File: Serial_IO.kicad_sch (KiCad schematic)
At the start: 39 parts

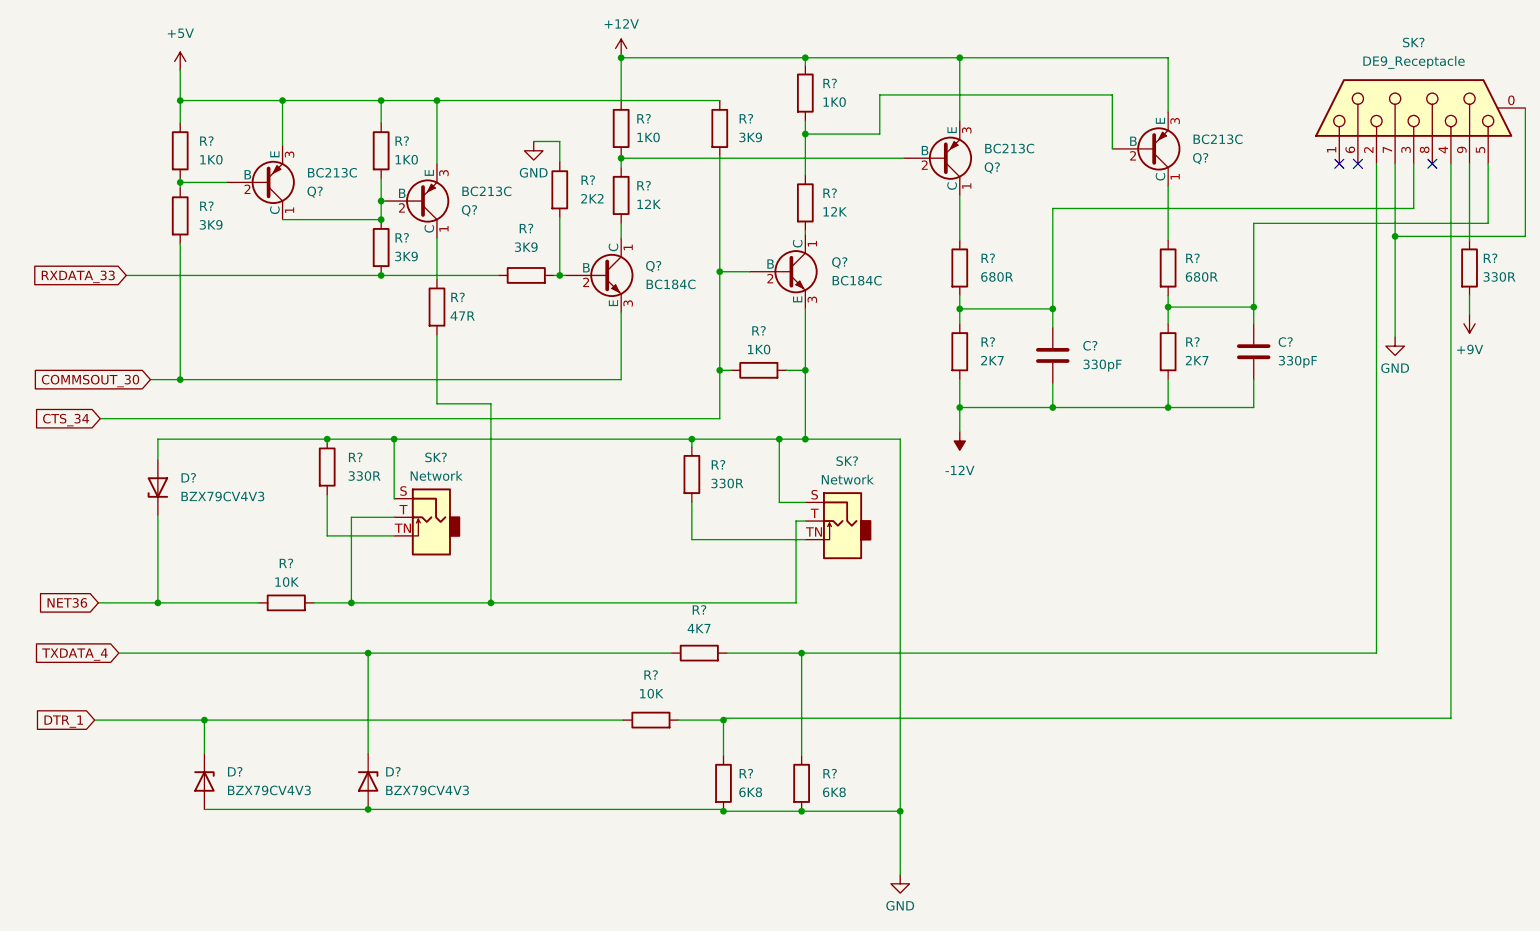
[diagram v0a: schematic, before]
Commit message: Add files via upload
Updated with Kicad 9. Now includes bom/ibom.html (Interactice BOM)
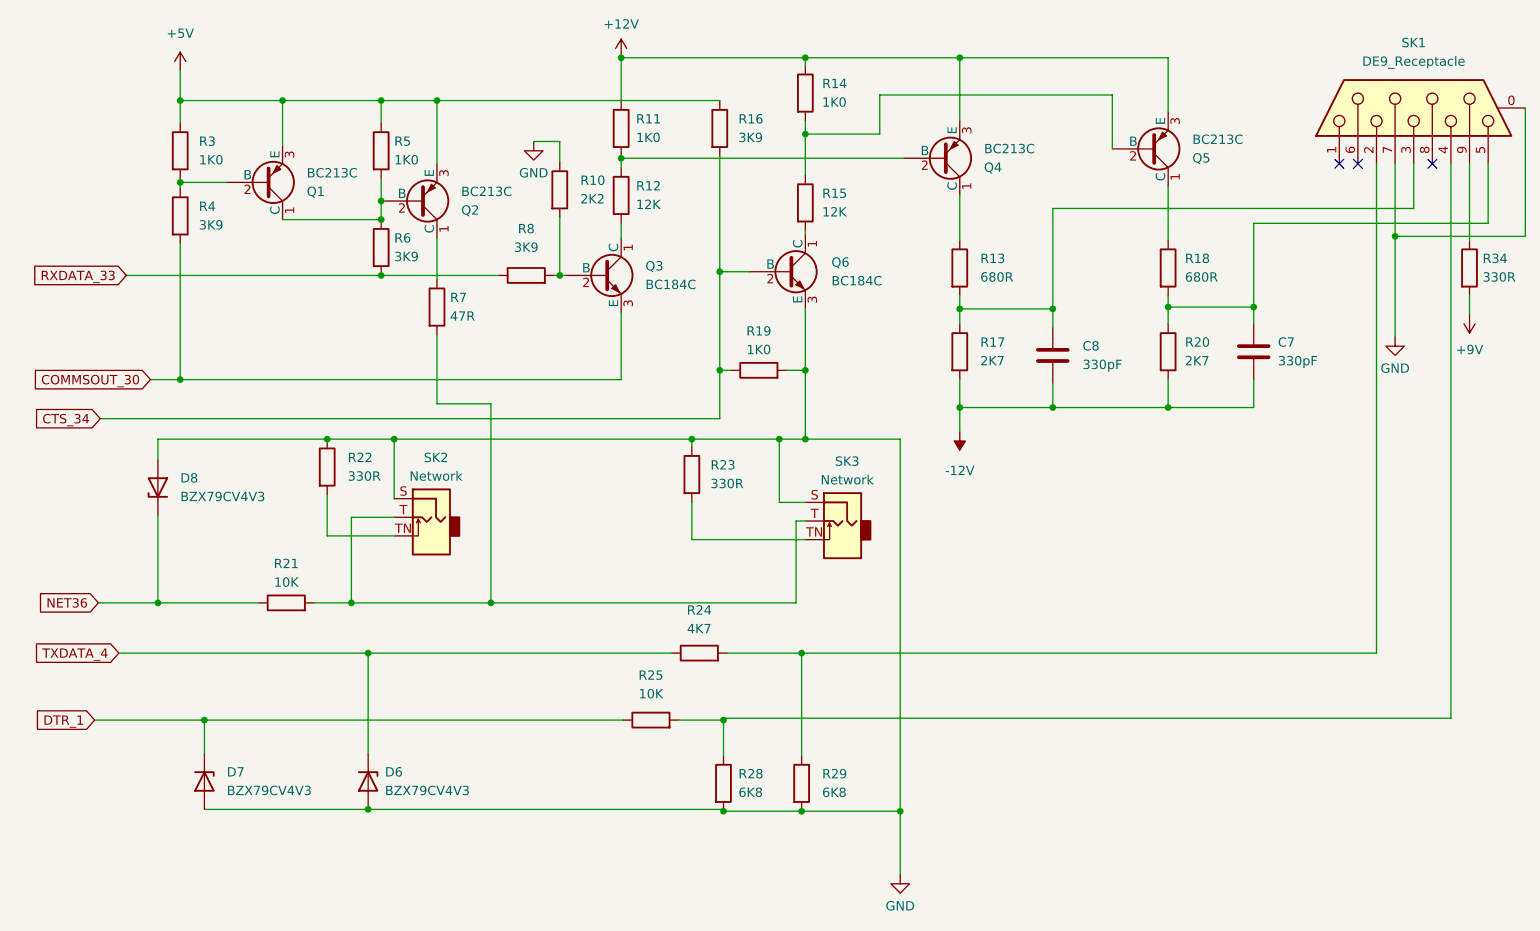
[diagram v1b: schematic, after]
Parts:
- C7, C8: renamed from C?; footprint Spectrum:Capacitor Ceramic -> Mod:Capacitor Ceramic
- D6, D7, D8: renamed from D?; footprint Spectrum:Diode 1N -> Mod:Diode 1N
- Q1, Q2, Q3, Q4, Q5, Q6: renamed from Q?; footprint Package_TO_SOT_THT:TO-92L_Inline_Wide -> Mod:TO-92L_Inline_Wide
- R10, R11, R12, R13, R14, R15, R16, R17, R18, R19, R20, R21, R22, R23, R24, R25, R28, R29, R3, R34, R4, R5, R6, R7, R8: renamed from R?; footprint Spectrum:Resistor_0.25W -> Mod:Resistor_0.25W
- SK1: renamed from SK?; footprint Connector_Dsub:DSUB-9_Female_Horizontal_P2.77x2.84mm_EdgePinOffset14.56mm_Housed_MountingHolesOffset15.98mm -> Mod:DSUB-9_Female_Horizontal_P2.77x2.84mm_EdgePinOffset14.56mm_Housed_MountingHolesOffset15.98mm
- SK2, SK3: renamed from SK?; footprint ZX Spectrum 3.5mm:ZX Spectrum 3.5mm Skt -> Mod:ZX Spectrum 3.5mm Skt
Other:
- company: (none) -> Drawn by liveboxandy
- title: ZX Interface 1 Schematic -> ZX Interface 1 Schematic - Sinclair Labels
